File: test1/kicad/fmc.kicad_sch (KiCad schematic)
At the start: 4 parts, among them J1 FMC LPC (C), J2 FMC LPC (D), J3 FMC LPC (G), J4 FMC LPC (H)

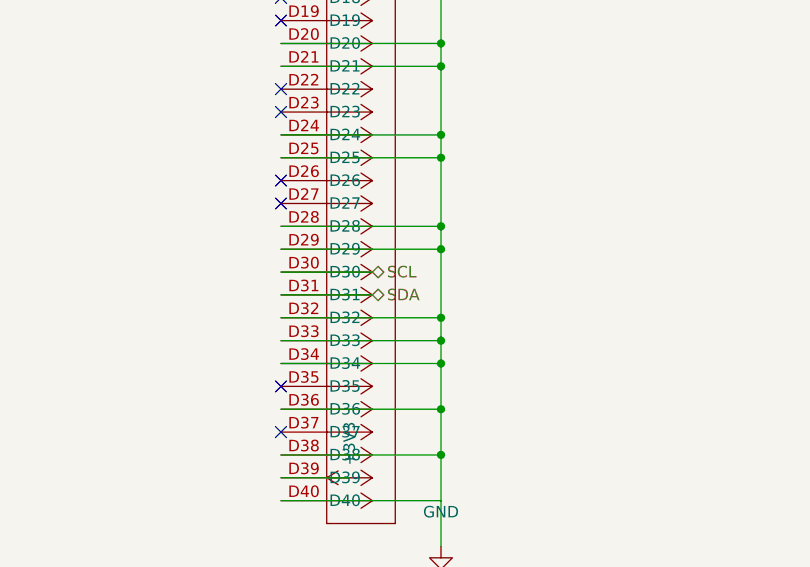
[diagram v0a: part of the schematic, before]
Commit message: Project-wide connectivity audit: refdes uniqueness + hier-label correctness
Added test1/verify_project.py as a kicad-cli-erc substitute (the dev
build doesn't ship _cvpcb.kiface, so sch erc is broken). The verifier
parses all .kicad_sch files and checks:
  1. Duplicate refdes (KiCad's refdes namespace is project-wide).
  2. Parent sheet-pin name + direction matches child hierarchical_label.
  3. Orphan child hierarchical_labels (no matching parent pin).

First run flagged 48 issues. Now reports 0.

Refdes scheme — per-sheet decade ranges so global namespace stays unique:
  FMC 1-9 (J1-J4)
  Power 10-19 (U10/U11, R10/R11, C10-C16, J10-J12)
  Bobcat 20-29 (U20, R20/R21, C20-C25)
  EEPROM 30-39 (U30, R30/R31, C30)
  Bias 40-49 (U40/U41 [U41 dual-unit OPA], Q40-Q43, R40/R41, C40-C43)
  Connectors 50-59 (J50-J57, TP50-TP52)

Hierarchical / global label rework:
  - Parent sheet-pin directions corrected to match child labels (was
    flipped on every Bobcat SPI pin and on FMC's LDO_EN/LSW_EN/LDO_PG).
  - Bobcat SPI labels: passive → input/output as appropriate.
  - Project-wide nets converted to global_label (auto-tie by name, no
    parent pins): SCL, SDA, SAMPLE_OUT*, OSC_EN, WEIGHT_EN, SAMPLE_TRIG,
    BIAS_ISO0/1, CS_L, SCLK, MOSI, MISO, SPI_DMODE, RESET_N.
  - hier_label retained for clean 2-sheet pairs: VADJ, LDO_EN, LDO_PG,
    LSW_EN (FMC ↔ Power); BIAS0/1 (Bias ↔ Bobcat); CLK_OUT0-3, GPIO0-3
    (Bobcat ↔ Connectors).
  - Visual cue in renders: globals render as boxed rectangles; hierarchical
    labels render as arrows — handy when scanning a sheet.

Memory: appended five connectivity-correctness lessons to
feedback_kicad_generator_lessons.md (refdes namespace, parent/child
direction parity, no-passive-for-real-signals, global vs hier decision
table, verify-after-every-change).

Co-Authored-By: Claude Opus 4.7 (1M context) <noreply@anthropic.com>
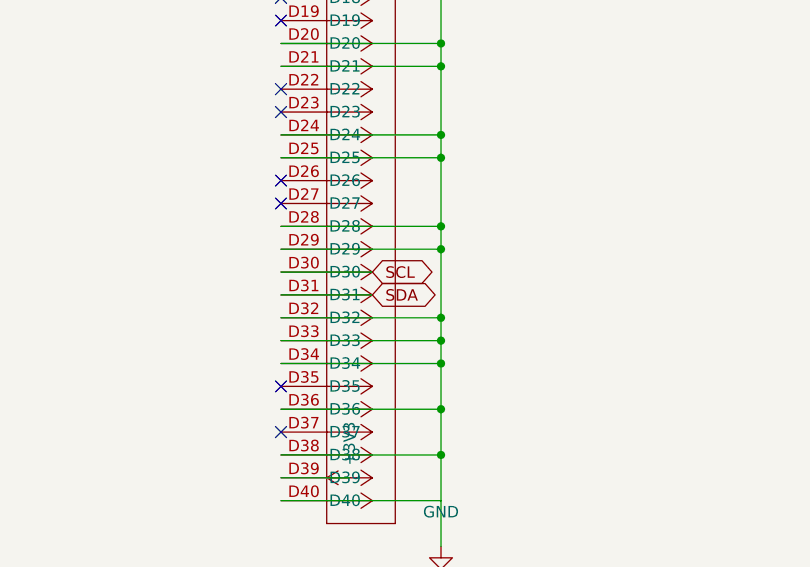
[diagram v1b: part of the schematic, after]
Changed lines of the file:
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@@
   (hierarchical_label "VADJ" (shape output) (at 270.16 191.52 0) (effects (font (size 1.27 1.27)) (justify left)))
   (wire (pts (xy 140.0 168.66) (xy 150.16 168.66)) (stroke (width 0) (type default)))
-  (hierarchical_label "SCL" (shape bidirectional) (at 150.16 168.66 0) (effects (font (size 1.27 1.27)) (justify left)))
+  (global_label "SCL" (shape bidirectional) (at 150.16 168.66 0) (effects (font (size 1.27 1.27)) (justify left)))
   (wire (pts (xy 140.0 171.2) (xy 150.16 171.2)) (stroke (width 0) (type default)))
-  (hierarchical_label "SDA" (shape bidirectional) (at 150.16 171.2 0) (effects (font (size 1.27 1.27)) (justify left)))
+  (global_label "SDA" (shape bidirectional) (at 150.16 171.2 0) (effects (font (size 1.27 1.27)) (justify left)))
   (wire (pts (xy 260.0 97.54) (xy 267.62 97.54)) (stroke (width 0) (type default)))
   (symbol
@@
       (project "test1"
         (path "/4ed7a046-ef33-57d9-8730-321c05965af3/e2abb566-d978-5c75-82ca-1f71ca6b792e" (reference "#PWRa990850a") (unit 1)))))
-  (no_connect (at 200.0 140.72))
-  (no_connect (at 80.0 161.04))
+  (no_connect (at 140.0 128.02))
+  (no_connect (at 140.0 150.88))
+  (no_connect (at 80.0 143.26))
+  (no_connect (at 140.0 110.24))
+  (no_connect (at 200.0 150.88))
+  (no_connect (at 200.0 173.74))
+  (no_connect (at 260.0 117.86))
+  (no_connect (at 260.0 140.72))
+  (no_connect (at 140.0 138.18))
+  (no_connect (at 140.0 161.04))
+  (no_connect (at 200.0 133.1))
+  (no_connect (at 200.0 155.96))
+  (no_connect (at 260.0 100.08))
+  (no_connect (at 200.0 178.82))
+  (no_connect (at 260.0 122.94))
+  (no_connect (at 80.0 130.56))
+  (no_connect (at 140.0 97.54))
+  (no_connect (at 80.0 153.42))
   (no_connect (at 140.0 120.4))
-  (no_connect (at 200.0 163.58))
-  (no_connect (at 200.0 186.44))
-  (no_connect (at 260.0 125.48))
-  (no_connect (at 260.0 148.34))
-  (no_connect (at 80.0 120.4))
-  (no_connect (at 80.0 143.26))
-  (no_connect (at 140.0 148.34))
-  (no_connect (at 260.0 107.7))
-  (no_connect (at 260.0 130.56))
-  (no_connect (at 80.0 102.62))
-  (no_connect (at 200.0 105.16))
-  (no_connect (at 200.0 128.02))
-  (no_connect (at 140.0 107.7))
-  (no_connect (at 200.0 150.88))
-  (no_connect (at 140.0 130.56))
-  (no_connect (at 200.0 173.74))
-  (no_connect (at 200.0 110.24))
-  (no_connect (at 80.0 130.56))
-  (no_connect (at 200.0 133.1))
-  (no_connect (at 80.0 153.42))
-  (no_connect (at 200.0 155.96))
-  (no_connect (at 140.0 158.5))
-  (no_connect (at 260.0 117.86))
+  (no_connect (at 260.0 176.28))
   (no_connect (at 80.0 112.78))
   (no_connect (at 80.0 135.64))
-  (no_connect (at 260.0 171.2))
   (no_connect (at 80.0 158.5))
-  (no_connect (at 140.0 117.86))
-  (no_connect (at 140.0 140.72))
-  (no_connect (at 260.0 100.08))
-  (no_connect (at 260.0 153.42))
   (no_connect (at 200.0 120.4))
-  (no_connect (at 260.0 176.28))
-  (no_connect (at 140.0 100.08))
+  (no_connect (at 200.0 143.26))
+  (no_connect (at 200.0 166.12))
+  (no_connect (at 260.0 110.24))
+  (no_connect (at 200.0 188.98))
+  (no_connect (at 140.0 107.7))
+  (no_connect (at 140.0 130.56))
+  (no_connect (at 260.0 163.58))
   (no_connect (at 200.0 102.62))
+  (no_connect (at 260.0 186.44))
+  (no_connect (at 200.0 125.48))
+  (no_connect (at 200.0 148.34))
+  (no_connect (at 200.0 171.2))
   (no_connect (at 80.0 122.94))
-  (no_connect (at 200.0 125.48))
   (no_connect (at 80.0 145.8))
-  (no_connect (at 140.0 128.02))
-  (no_connect (at 200.0 178.82))
-  (no_connect (at 80.0 105.16))
-  (no_connect (at 260.0 140.72))
-  (no_connect (at 80.0 128.02))
-  (no_connect (at 260.0 163.58))
-  (no_connect (at 80.0 150.88))
-  (no_connect (at 260.0 186.44))
-  (no_connect (at 140.0 110.24))
-  (no_connect (at 260.0 122.94))
   (no_connect (at 260.0 145.8))
   (no_connect (at 260.0 168.66))
-  (no_connect (at 200.0 143.26))
-  (no_connect (at 200.0 166.12))
-  (no_connect (at 200.0 188.98))
-  (no_connect (at 80.0 115.32))
-  (no_connect (at 140.0 97.54))
-  (no_connect (at 200.0 148.34))
-  (no_connect (at 200.0 171.2))
-  (no_connect (at 140.0 150.88))
-  (no_connect (at 260.0 110.24))
+  (no_connect (at 80.0 105.16))
+  (no_connect (at 80.0 128.02))
+  (no_connect (at 80.0 150.88))
+  (no_connect (at 200.0 112.78))
+  (no_connect (at 140.0 148.34))
+  (no_connect (at 200.0 135.64))
+  (no_connect (at 200.0 158.5))
+  (no_connect (at 200.0 181.36))
   (no_connect (at 260.0 133.1))
   (no_connect (at 260.0 155.96))
   (no_connect (at 260.0 178.82))
+  (no_connect (at 200.0 117.86))
+  (no_connect (at 200.0 140.72))
+  (no_connect (at 200.0 163.58))
+  (no_connect (at 80.0 115.32))
+  (no_connect (at 80.0 138.18))
   (no_connect (at 260.0 115.32))
   (no_connect (at 260.0 138.18))
   (no_connect (at 260.0 161.04))
   (no_connect (at 260.0 183.9))
-  (no_connect (at 200.0 112.78))
-  (no_connect (at 200.0 135.64))
-  (no_connect (at 200.0 158.5))
-  (no_connect (at 140.0 138.18))
-  (no_connect (at 200.0 181.36))
-  (no_connect (at 140.0 161.04))
-  (no_connect (at 200.0 117.86))
-  (no_connect (at 80.0 138.18))
+  (no_connect (at 140.0 158.5))
+  (no_connect (at 80.0 120.4))
+  (no_connect (at 140.0 117.86))
+  (no_connect (at 200.0 105.16))
+  (no_connect (at 140.0 140.72))
+  (no_connect (at 200.0 128.02))
+  (no_connect (at 80.0 102.62))
+  (no_connect (at 260.0 125.48))
+  (no_connect (at 260.0 148.34))
+  (no_connect (at 140.0 100.08))
+  (no_connect (at 260.0 171.2))
+  (no_connect (at 200.0 110.24))
+  (no_connect (at 260.0 107.7))
+  (no_connect (at 200.0 186.44))
+  (no_connect (at 260.0 130.56))
+  (no_connect (at 260.0 153.42))
+  (no_connect (at 80.0 161.04))
   (sheet_instances
     (path "/" (page "2"))

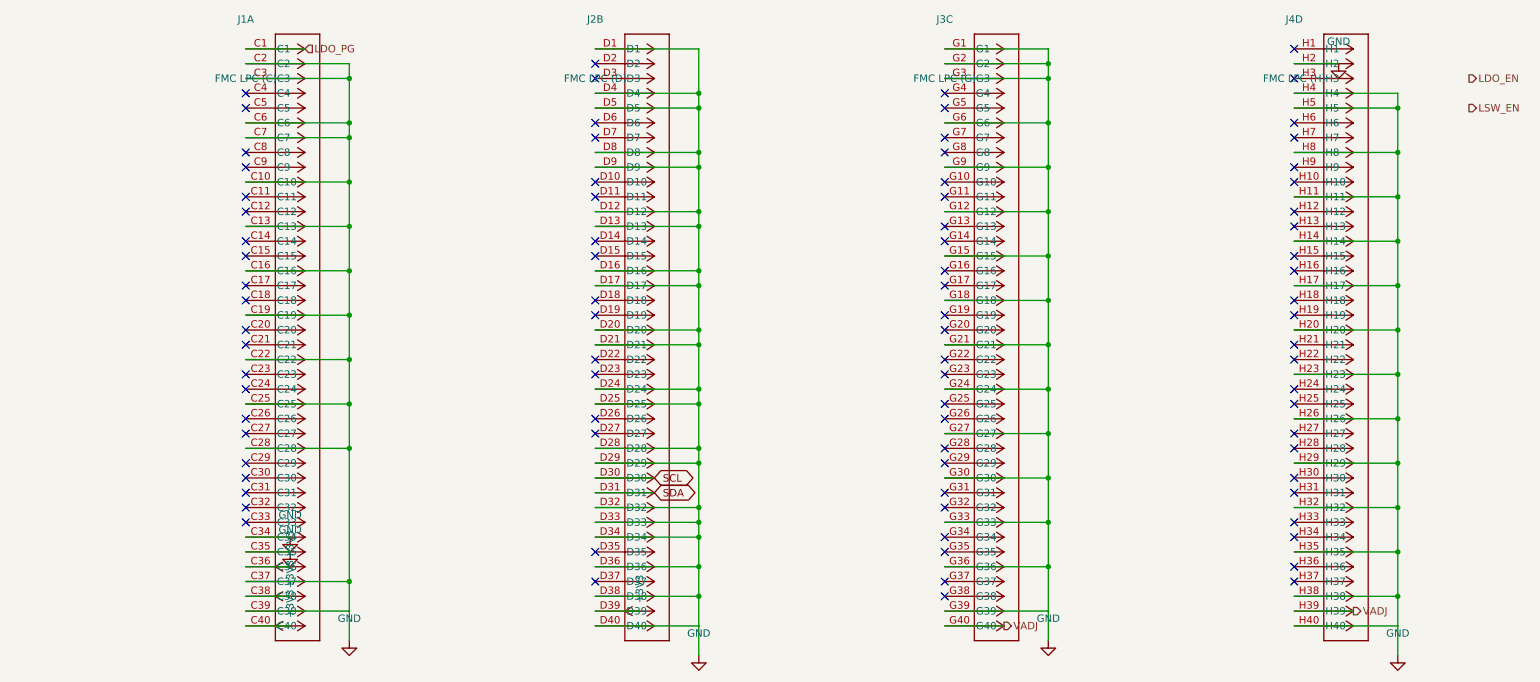
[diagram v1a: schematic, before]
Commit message: Split test1 generator into per-sheet package with netlist YAML + strict validator
Combines three layered changes:

1. Apply the design-review audit (test1/error_log.md): 9 ERRORs + 10
   WARNINGs from the new .claude/skills/design_review.md skill — FMC
   LA-bank 0Ω routing, Bobcat SPI/control/GPIO pull network, LDO
   ANY-OUT to FPGA, LDO_PG pull-up + series, bias DNP convention,
   kelvin SNS, per-pin VDDIO + bulk caps, BIAS bypass, VADJ/VDDIO bulk,
   MCP4728 EEPROM provisioning notes, shared-rail decision documented.

2. Refactor test1/gen_schematic.py (1825 lines → 138-line entry point)
   into a per-sheet package at test1/gen/:
     config.py / symbols.py / shared.py  — primitives, Sheet container,
     LA_ASSIGN, footprints, sexpr emit
     build_<sheet>.py × 7                — one builder per child sheet
     netlist.py / validator.py           — YAML loader + strict checker
   Per-session context for any single sheet drops to ~500 lines.
   Also sorts non-deterministic set iteration that made fmc.kicad_sch
   diff noisily across runs.

3. Add a declarative connectivity layer (netlist/<sheet>.yaml):
   parts inventory + nets (power / hier / global / internal), with
   explicit unit syntax for multi-unit symbols (U41:u2.7, J3:u3.G16).
   The strict validator runs at the end of every build_<sheet>() call:
     - inventory: YAML parts ↔ placed (refdes, unit) parity
     - connectivity: every YAML net member is in a connected component
       named the YAML net name (Union-Find on wires + junctions + label
       anchors + power-symbol pins; T-intersections auto-connect)
     - internal nets: members in one component, no name check
   Sheet now records structured PlacedPart/wire/label data alongside
   the s-expr emit; validator reads those instead of re-parsing.

All 6 child sheets' .kicad_sch outputs are byte-identical to the
post-design-review reference, and verify_project.py reports 0 issues.

Co-Authored-By: Claude Opus 4.7 (1M context) <noreply@anthropic.c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
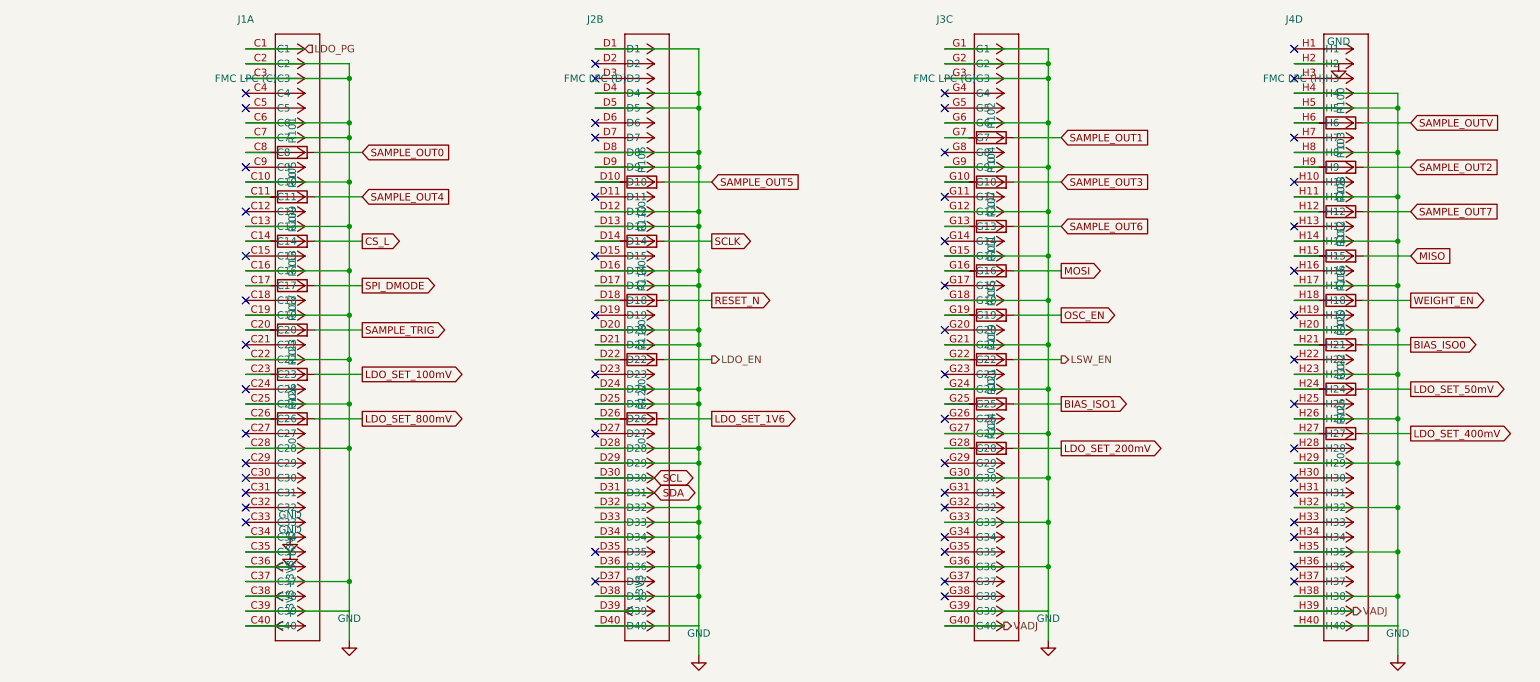
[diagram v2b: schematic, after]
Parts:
- added R100, R101, R102, R103, R104, R105, R106, R107, R108, R109, R110, R111, R112, R113, R114, R115, R116, R117, R118, R119, R120, R121, R122, R123, R124, R125, R126, R127: 0, Resistor_SMD:R_0402_1005Metric, symbol Device:R
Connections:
- net LDO_EN: now also R118.2
- net LSW_EN: now also R119.2
- net at J4.H12: now also R108.1
- net at J4.H15: now also R112.1
- net at J4.H18: now also R116.1
- net at J4.H21: now also R120.1
- net at J4.H24: now also R122.1
- net at J4.H27: now also R125.1
- net at J4.H6: now also R100.1
- net at J4.H9: now also R103.1
- net at J2.D10: now also R106.1
- net at J2.D14: now also R110.1
- net at J2.D18: now also R114.1
- net at J2.D22: now also R118.1
- net at J2.D26: now also R127.1
- net at J1.C11: now also R105.1
- net at J1.C14: now also R109.1
- net at J1.C17: now also R113.1
- net at J1.C20: now also R117.1
- net at J1.C23: now also R123.1
- net at J1.C26: now also R126.1
- net at J1.C8: now also R101.1
- net at J3.G10: now also R104.1
- net at J3.G13: now also R107.1
- net at J3.G16: now also R111.1
- net at J3.G19: now also R115.1
- net at J3.G22: now also R119.1
- net at J3.G25: now also R121.1
- net at J3.G28: now also R124.1
- net at J3.G7: now also R102.1
- new net BIAS_ISO0: R120.2
- new net BIAS_ISO1: R121.2
- new net CS_L: R109.2
- new net LDO_SET_100mV: R123.2
- new net LDO_SET_1V6: R127.2
- new net LDO_SET_200mV: R124.2
- new net LDO_SET_400mV: R125.2
- new net LDO_SET_50mV: R122.2
- new net LDO_SET_800mV: R126.2
- new net MISO: R112.2
- new net MOSI: R111.2
- new net OSC_EN: R115.2
- new net RESET_N: R114.2
- new net SAMPLE_OUT0: R101.2
- new net SAMPLE_OUT1: R102.2
- new net SAMPLE_OUT2: R103.2
- new net SAMPLE_OUT3: R104.2
- new net SAMPLE_OUT4: R105.2
- new net SAMPLE_OUT5: R106.2
- new net SAMPLE_OUT6: R107.2
- new net SAMPLE_OUT7: R108.2
- new net SAMPLE_OUTV: R100.2
- new net SAMPLE_TRIG: R117.2
- new net SCLK: R110.2
- new net SPI_DMODE: R113.2
- new net WEIGHT_EN: R116.2
- no-connect marks 85 -> 57

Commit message: Add layout linter + cluster helpers; fix silent shorts across sheets
Introduces gen/layout_lint.py with checks for bbox spacing, wires
through/into a body, parallel-wire overlap on the same axis, bridged
drop columns, and dense GND clusters — non-fatal warnings the strict
validator cannot catch (each net's name is still present in a bridged
component's name set, so per-member name checks pass).

Fixes the bugs the linter exposed:
- FMC routing flipped to exit LEFT (pin-protrusion side) so wires no
  longer pass through the connector body
- bobcat OWT (pins 23-25) + GPIO (37-40) get one drop column per pin,
  ending the silent shorts between adjacent nets
- bobcat SPI pin 14 pull-x shifted off pin 19's column
- bias Q40/Q41 source/drain wires detoured around the body so source
  no longer shorts to drain through the same vertical
- power LDO redundant tap stubs + GND-rail dupes removed; C12 moved
  off R10's column so NR_SS doesn't short to GND
- C11 ↔ R10, J54-56 ↔ R50-52 spacing widened to meet bbox rule

Adds gnd_bus() and decoupling_cluster() helpers in gen/shared.py and
applies gnd_bus() to the eeprom address-strap pins.

Skill doc gets rules for pin-protrusion side, per-pin drop columns,
and same-axis wire overlap. All 7 sheets now pass kicad-cli parse,
the strict connectivity validator, and the layout linter.

Co-Authored-By: Claude Opus 4.7 (1M context) <noreply@anthropic.com>
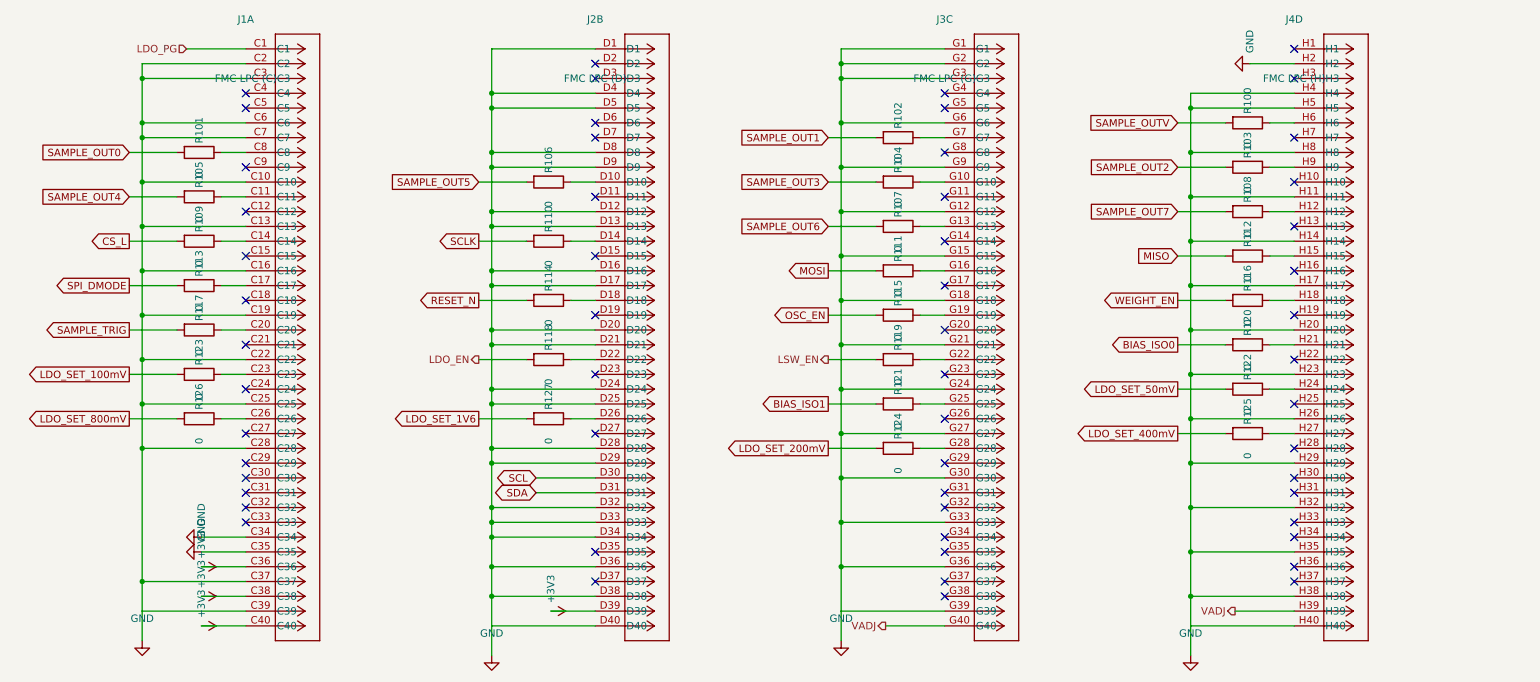
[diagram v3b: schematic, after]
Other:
- moved on the sheet: R100, R101, R102, R103, R104, R105, R106, R107, R108, R109, R110, R111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
